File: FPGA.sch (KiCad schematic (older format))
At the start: 8 parts, among them U13 ADS1015, U14 SiT8008B, U8 GW1N-9LQ100

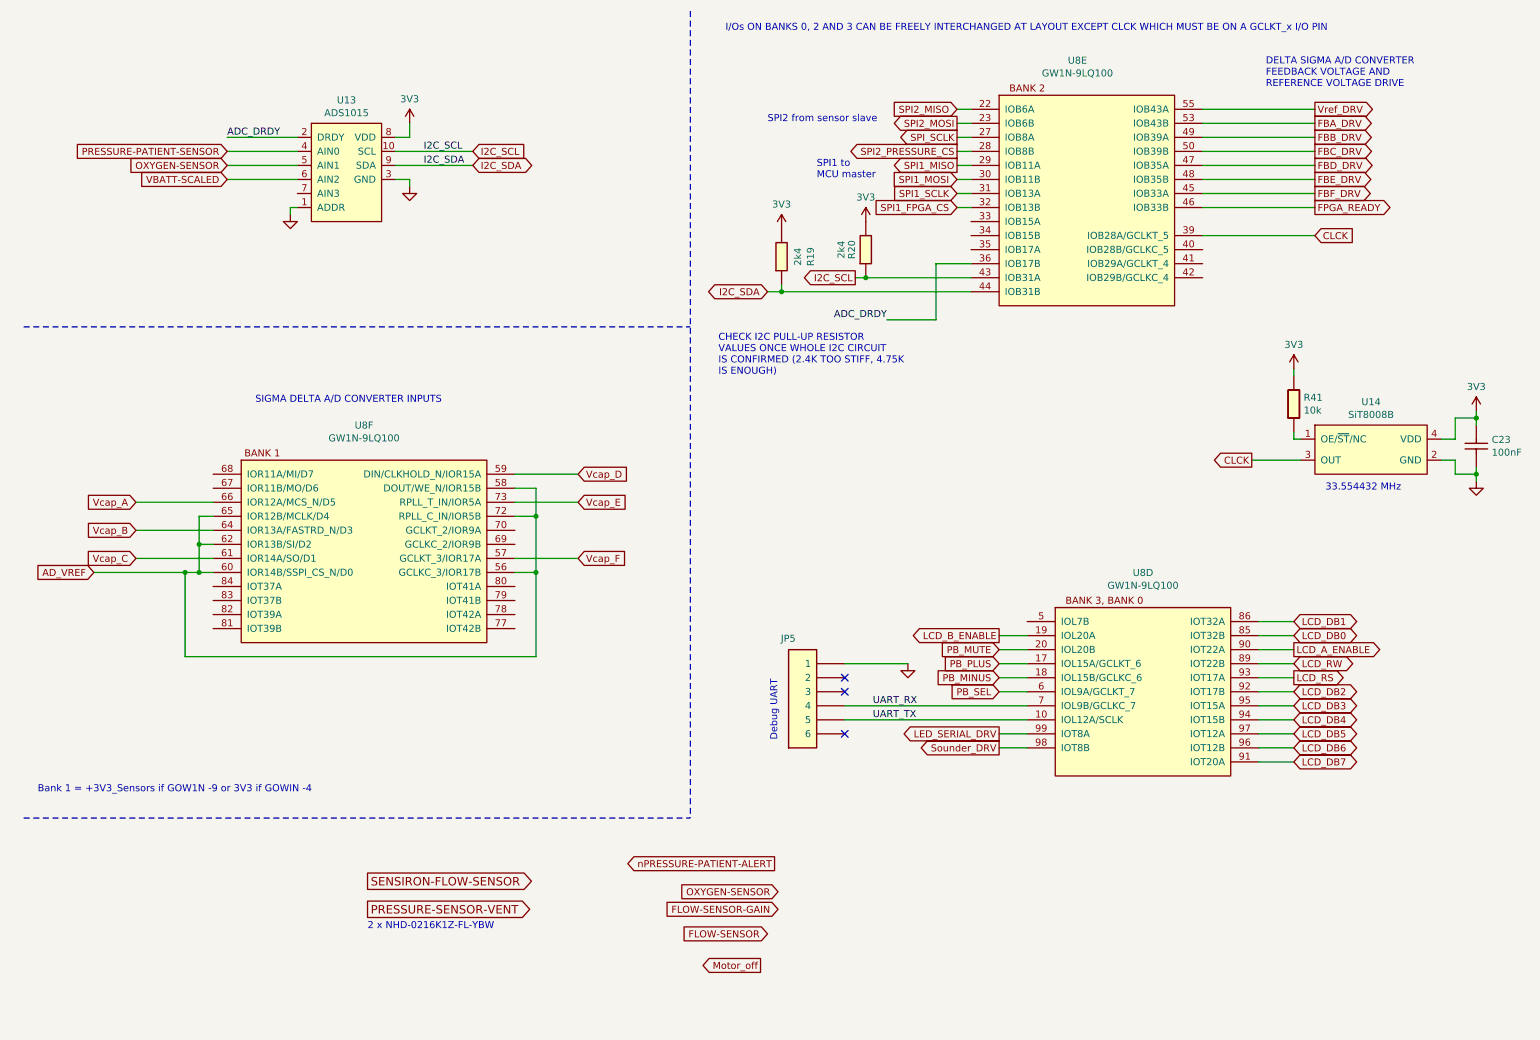
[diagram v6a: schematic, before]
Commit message: Removed second Vref from U9 on ADC page, replaced with additional 8th input, G
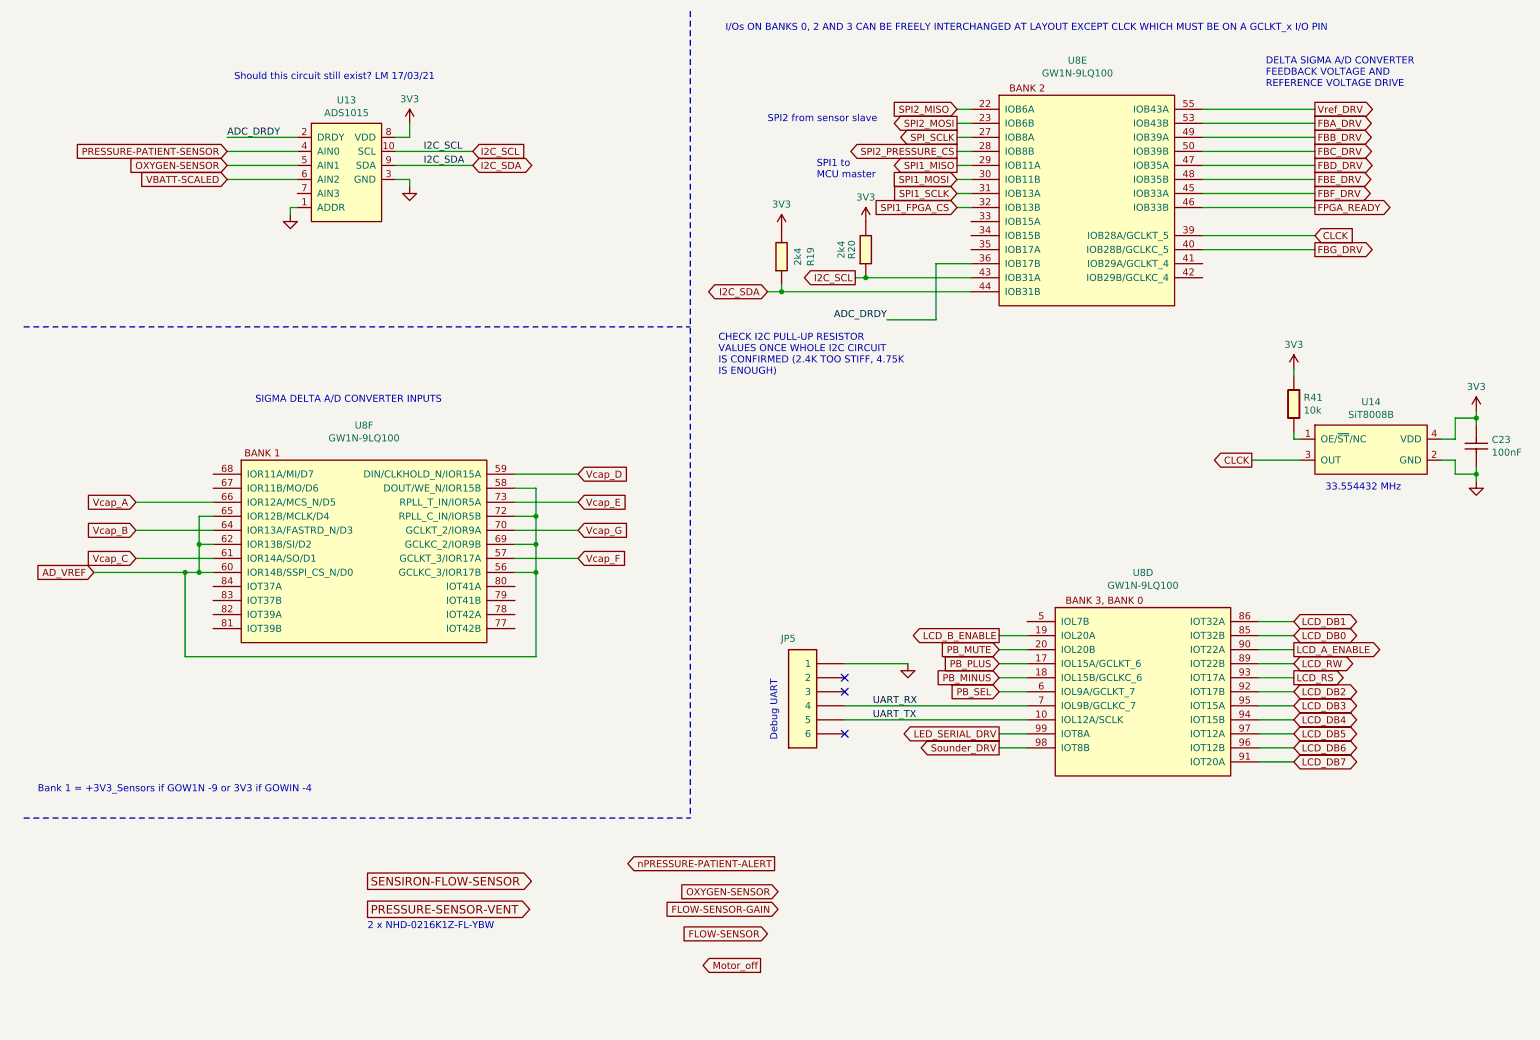
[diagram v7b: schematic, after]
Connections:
- net AD_VREF: now also U8.69 (GCLKC_2/IOR9B)
- net Vcap_G: now reaches U8.70 (GCLKT_2/IOR9A)
- net FBG_DRV: now reaches U8.40 (IOB28B/GCLKC_5)
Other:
- note added: "Should this circuit still exist? LM 17/03/21"
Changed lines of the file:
@@
 Connection ~ 4150 4500
 Wire Wire Line
-	4150 4100 4150 4500
+	4150 4100 4150 4300
 Wire Wire Line
 	4450 3800 4000 3800
@@
 Wire Wire Line
 	8900 2100 9700 2100
+Text GLabel 9700 2200 2    50   Output ~ 0
+FBG_DRV
+Wire Wire Line
+	8900 2200 9700 2200
+Text GLabel 4450 4200 2    50   Input ~ 0
+Vcap_G
+Wire Wire Line
+	4450 4200 4000 4200
+Wire Wire Line
+	4000 4300 4150 4300
+Connection ~ 4150 4300
+Wire Wire Line
+	4150 4300 4150 4500
+Text Notes 2000 1000 0    50   ~ 0
+Should this circuit still exist? LM 17/03/21
 $EndSCHEMATC

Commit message: Update FPGA.sch
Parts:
- added TVS-D3, TVS-D4: ESD5Z3.3T1G, SODFL1608X70N, symbol OpenVent:ESD5Z3.3T1G
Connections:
- wire segments 97 -> 104
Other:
- moved on the sheet: JP5
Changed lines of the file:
@@
 Comment4 ""
 $EndDescr
-Text GLabel 5850 6575 0    50   Output ~ 0
+Text GLabel 5650 6625 0    50   Output ~ 0
 nPRESSURE-PATIENT-ALERT
 Text GLabel 7450 5750 0    50   Output ~ 0
 Sounder_DRV
-Text GLabel 7450 5650 0    50   Output ~ 0
-LED_SERIAL_DRV
 $Comp
 L OpenVent:SiT8008B U14
@@
 	1    0    0    -1
 $EndComp
-Text Notes 5875 5700 1    50   ~ 0
-Debug UART
-NoConn ~ 6350 5350
-NoConn ~ 6350 5250
-NoConn ~ 6350 5650
-$Comp
-L OpenVent:Pin_Header,_1x6-Way,_2.54mm_Pitch JP?
-U 1 1 5FD254BC
-P 6350 5650
-AR Path="/5F988182/5FD254BC" Ref="JP?"  Part="1"
-AR Path="/5F8F894A/5FD254BC" Ref="JP5"  Part="1"
-F 0 "JP5" H 6700 6300 50  0000 L BNN
-F 1 "Pin_Header,_1x6-Way,_2.54mm_Pitch" H 6350 5650 50  0001 C CNN
-F 2 "Connector_PinHeader_2.54mm:PinHeader_1x06_P2.54mm_Vertical" H 6350 5650 50  0001 C CNN
-F 3 "" H 6350 5650 50  0001 C CNN
-	1    6350 5650
-	-1   0    0    -1
-$EndComp
-Text Label 6550 5450 0    50   ~ 0
-UART_RX
-Text Label 6550 5550 0    50   ~ 0
-UART_TX
 Text Notes 9775 3925 0    50   ~ 0
 33.554432 MHz
-$Comp
-L OpenVent:GND #PWR032
-U 1 1 5FD3A041
-P 6800 5150
-F 0 "#PWR032" H 6800 4900 50  0001 C CNN
-F 1 "GND" H 6800 5000 50  0001 C CNN
-F 2 "" H 6800 5150 50  0001 C CNN
-F 3 "" H 6800 5150 50  0001 C CNN
-	1    6800 5150
-	1    0    0    -1
-$EndComp
 Text Label 6650 2700 2    50   ~ 0
 ADC_DRDY
@@
 	1    0    0    -1
 $EndComp
-Wire Wire Line
-	6800 5150 6350 5150
 $Comp
 L OpenVent:10k_0603_Chip_Resistor,_1%,_0.1W R41
@@
 Text GLabel 2950 6900 2    60   Output ~ 0
 PRESSURE-SENSOR-VENT
-Text GLabel 5800 7075 0    50   Input ~ 0
+Text GLabel 5600 7125 0    50   Input ~ 0
 FLOW-SENSOR
-Text GLabel 5875 6775 0    50   Input ~ 0
+Text GLabel 5675 6825 0    50   Input ~ 0
 OXYGEN-SENSOR
-Text GLabel 5875 6900 0    50   Input ~ 0
+Text GLabel 5675 6950 0    50   Input ~ 0
 FLOW-SENSOR-GAIN
 Text GLabel 2950 6700 2    60   Output ~ 0
 SENSIRON-FLOW-SENSOR
-Text GLabel 5750 7300 0    50   Output ~ 0
+Text GLabel 5550 7350 0    50   Output ~ 0
 Motor_off
 Text GLabel 7450 5050 0    50   Input ~ 0
@@
 Wire Wire Line
 	7450 5350 7650 5350
-Wire Wire Line
-	6350 5450 7650 5450
-Wire Wire Line
-	6350 5550 7650 5550
 Text Notes 5500 650  0    50   ~ 0
 I/Os ON BANKS 0, 2 AND 3 CAN BE FREELY INTERCHANGED AT LAYOUT EXCEPT CLCK WHICH MUST BE ON A GCLKT_x I/O PIN
@@
 Text Notes 2000 1000 0    50   ~ 0
 Should this circuit still exist? LM 17/03/21
+$Comp
+L OpenVent:GND #PWR032
+U 1 1 5FD3A041
+P 6200 5150
+F 0 "#PWR032" H 6200 4900 50  0001 C CNN
+F 1 "GND" H 6200 5000 50  0001 C CNN
+F 2 "" H 6200 5150 50  0001 C CNN
+F 3 "" H 6200 5150 50  0001 C CNN
+	1    6200 5150
+	1    0    0    -1
+$EndComp
+Text Label 6550 5550 0    50   ~ 0
+UART_TX
+Text Label 6550 5450 0    50   ~ 0
+UART_RX
+$Comp
+L OpenVent:Pin_Header,_1x6-Way,_2.54mm_Pitch JP?
+U 1 1 5FD254BC
+P 5900 5650
+AR Path="/5F988182/5FD254BC" Ref="JP?"  Part="1"
+AR Path="/5F8F894A/5FD254BC" Ref="JP5"  Part="1"
+F 0 "JP5" H 6250 6300 50  0000 L BNN
+F 1 "Pin_Header,_1x6-Way,_2.54mm_Pitch" H 5900 5650 50  0001 C CNN
+F 2 "Connector_PinHeader_2.54mm:PinHeader_1x06_P2.54mm_Vertical" H 5900 5650 50  0001 C CNN
+F 3 "" H 5900 5650 50  0001 C CNN
+	1    5900 5650
+	-1   0    0    -1
+$EndComp
+NoConn ~ 5900 5650
+NoConn ~ 5900 5250
+NoConn ~ 5900 5350
+Text Notes 5425 5700 1    50   ~ 0
+Debug UART
+Text GLabel 7450 5650 0    50   Output ~ 0
+LED_SERIAL_DRV
+Wire Wire Line
+	6200 5150 5900 5150
+Wire Wire Line
+	5900 5550 6400 5550
+Wire Wire Line
+	5900 5450 6150 5450
+$Comp
+L OpenVent:ESD5Z3.3T1G TVS-D3
+U 1 1 6058ED6E
+P 6400 5750
+F 0 "TVS-D3" V 6654 5880 50  0000 L CNN
+F 1 "ESD5Z3.3T1G" V 6745 5880 50  0000 L CNN
+F 2 "SODFL1608X70N" H 6850 5750 50  0001 L CNN
+F 3 "http://www.onsemi.com/pub/Collateral/ESD5Z2.5T1-D.PDF" H 6850 5650 50  0001 L CNN
+F 4 "TVS Diode Uni-Direct. 240W 3.3V SOD-523 ON Semiconductor ESD5Z3.3T1G Uni-Directional TVS Diode, 200W peak, 2-Pin SOD-523" H 6850 5550 50  0001 L CNN "Description"
+F 5 "0.7" H 6850 5450 50  0001 L CNN "Height"
+F 6 "ON Semiconductor" H 6850 5350 50  0001 L CNN "Manufacturer_Name"
+F 7 "ESD5Z3.3T1G" H 6850 5250 50  0001 L CNN "Manufacturer_Part_Number"
+F 8 "863-ESD5Z3.3T1G" H 6850 5150 50  0001 L CNN "Mouser Part Number"
+F 9 "https://www.mouser.co.uk/ProductDetail/ON-Semiconductor/ESD5Z33T1G/?qs=OSf9jACorvaH3Y8oRWEcuQ%3D%3D" H 6850 5050 50  0001 L CNN "Mouser Price/Stock"
+F 10 "ESD5Z3.3T1G" H 6850 4950 50  0001 L CNN "Arrow Part Number"
+F 11 "https://www.arrow.com/en/products/esd5z3.3t1g/on-semiconductor" H 6850 4850 50  0001 L CNN "Arrow Price/Stock"
+	1    6400 5750
+	0    1    1    0
+$EndComp
+$Comp
+L OpenVent:ESD5Z3.3T1G TVS-D4
+U 1 1 6059146A
+P 6150 5750
+F 0 "TVS-D4" V 6404 5620 50  0000 R CNN
+F 1 "ESD5Z3.3T1G" V 6495 5620 50  0000 R CNN
+F 2 "SODFL1608X70N" H 6600 5750 50  0001 L CNN
+F 3 "http://www.onsemi.com/pub/Collateral/ESD5Z2.5T1-D.PDF" H 6600 5650 50  0001 L CNN
+F 4 "TVS Diode Uni-Direct. 240W 3.3V SOD-523 ON Semiconductor ESD5Z3.3T1G Uni-Directional TVS Diode, 200W peak, 2-Pin SOD-523" H 6600 5550 50  0001 L CNN "Description"
+F 5 "0.7" H 6600 5450 50  0001 L CNN "Height"
+F 6 "ON Semiconductor" H 6600 5350 50  0001 L CNN "Manufacturer_Name"
+F 7 "ESD5Z3.3T1G" H 6600 5250 50  0001 L CNN "Manufacturer_Part_Number"
+F 8 "863-ESD5Z3.3T1G" H 6600 5150 50  0001 L CNN "Mouser Part Number"
+F 9 "https://www.mouser.co.uk/ProductDetail/ON-Semiconductor/ESD5Z33T1G/?qs=OSf9jACorvaH3Y8oRWEcuQ%3D%3D" H 6600 5050 50  0001 L CNN "Mouser Price/Stock"
+F 10 "ESD5Z3.3T1G" H 6600 4950 50  0001 L CNN "Arrow Part Number"
+F 11 "https://www.arrow.com/en/products/esd5z3.3t1g/on-semiconductor" H 6600 4850 50  0001 L CNN "Arrow Price/Stock"
+	1    6150 5750
+	0    1    1    0
+$EndComp
+$Comp
+L OpenVent:GND #PWR?
+U 1 1 6059B6E0
+P 6300 6450
+F 0 "#PWR?" H 6300 6200 50  0001 C CNN
+F 1 "GND" H 6300 6300 50  0001 C CNN
+F 2 "" H 6300 6450 50  0001 C CNN
+F 3 "" H 6300 6450 50  0001 C CNN
+	1    6300 6450
+	1    0    0    -1
+$EndComp
+Wire Wire Line
+	6400 5750 6400 5550
+Connection ~ 6400 5550
+Wire Wire Line
+	6400 5550 7650 5550
+Wire Wire Line
+	6150 5750 6150 5450
+Connection ~ 6150 5450
+Wire Wire Line
+	6150 5450 7650 5450
+Wire Wire Line
+	6150 6350 6300 6350
+Wire Wire Line
+	6300 6450 6300 6350
+Connection ~ 6300 6350
+Wire Wire Line
+	6300 6350 6400 6350
 $EndSCHEMATC
